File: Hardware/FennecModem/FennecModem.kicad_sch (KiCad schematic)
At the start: 8 parts, among them SW101 RESET

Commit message: Bump fennec pcb
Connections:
- net TONE_OUT: now reaches A1.4 (GPIO2)
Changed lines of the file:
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@@
+		)
+	)
+	(wire
+		(pts
+			(xy 17.78 118.11) (xy 30.48 118.11)
+		)
+		(stroke
+			(width 0)
+			(type default)
 		)
 	)
@@
 		(pts
 			(xy 262.89 135.89) (xy 262.89 139.7)
+		)
+		(stroke
+			(width 0)
+			(type default)
+		)
+	)
+	(wire
+		(pts
+			(xy 185.42 21.59) (xy 201.93 21.59)
 		)
 		(stroke
@@
 		)
 	)
+	(label "TONE_OUT"
+		(at 185.42 21.59 0)
+		(effects
+			(font
+				(size 1.27 1.27)
+			)
+			(justify left bottom)
+		)
+	)
+	(label "TONE_OUT"
+		(at 17.78 118.11 0)
+		(effects
+			(font
+				(size 1.27 1.27)
+			)
+			(justify left bottom)
+		)
+	)

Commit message: Route!
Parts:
- removed D102: SCK, LED_SMD:LED_0805_2012Metric, symbol Device:LED
- removed R107: 330, Resistor_SMD:R_0805_2012Metric, symbol Device:R
- removed SW101: RESET, Button_Switch_THT:SW_PUSH_6mm_H5mm, symbol Switch:SW_Push
- added JP2, JP3, JP4, JP5, JP6: SolderJumper_2_Open, Jumper:SolderJumper-2_P1.3mm_Open_TrianglePad1.0x1.5mm, symbol Jumper:SolderJumper_2_Open
- A1: footprint Module:RaspberryPi_Pico_Common_Unspecified -> Module:RaspberryPi_Pico_Common_THT
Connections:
- net +5V: now also A1.39 (VSYS); no longer R103.2, R108.2
- net GND: now also A1.13 (GND), A1.18 (GND), A1.23 (GND), A1.28 (GND), A1.3 (GND), A1.38 (GND), A1.8 (GND), D101.1 (K)
- net RXD: now also A1.11 (GPIO8)
- net STAT: now also A1.9 (GPIO6), R103.2; no longer D101.1 (K)
- net TXD: now also A1.12 (GPIO9)
- net PTT: now reaches A1.14 (GPIO10)
- net Sleep: now reaches A1.15 (GPIO11)
- net H/L: now reaches A1.16 (GPIO12)
- net SQL: now reaches A1.17 (GPIO13)
- net SDO: now reaches A1.21 (GPIO16)
- net CARD_SEL: now reaches A1.22 (GPIO17)
- net SPI_CLK: now reaches A1.24 (GPIO18)
- net SDI: now reaches A1.25 (GPIO19)
- net at A1.26 (GPIO20): now also JP4.2 (B)
- net at A1.27 (GPIO21): now also JP5.2 (B)
- net at A1.29 (GPIO22): now also JP6.2 (B)
- net TONE_IN: now reaches A1.31 (GPIO26_ADC0)
- net GNDA: now reaches A1.33 (AGND)
- net +3.3V: now reaches A1.36 (3V3)
- net +3.3V: now also R108.2
- net at A1.6 (GPIO4): now also JP3.2 (B)
- net at A1.7 (GPIO5): now also JP2.2 (B)
- new net SCL: JP2.1 (A)
- new net SDA: JP3.1 (A)
- new net SPI2: JP4.1 (A)
- new net SPI3: JP5.1 (A)
- new net SPI4: JP6.1 (A)
- no-connect marks 0 -> 12
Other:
- sheet Backplane ports: added CARD_SEL, SPI_SDO; removed none
- moved on the sheet: A1, D101, R103

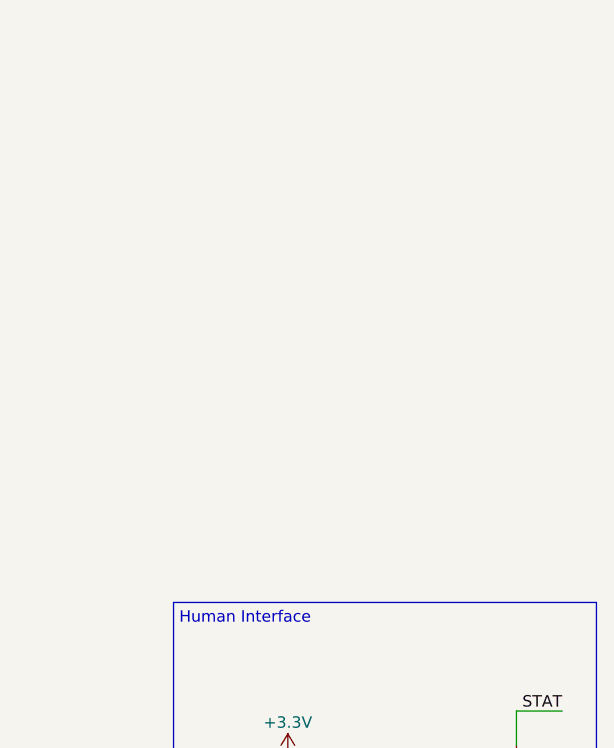
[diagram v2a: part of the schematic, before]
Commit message: Add stackup and fan
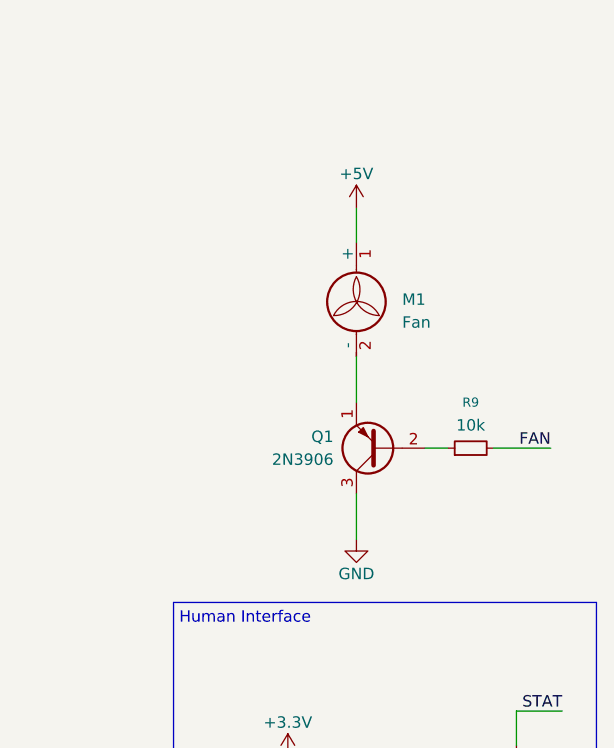
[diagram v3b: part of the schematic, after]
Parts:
- added M1: Fan, Connector_PinHeader_2.54mm:PinHeader_1x02_P2.54mm_Vertical, symbol Motor:Fan
- added Q1: 2N3906, Package_TO_SOT_THT:TO-92_Inline, symbol Transistor_BJT:2N3906
- added R9: 10k, Resistor_SMD:R_0805_2012Metric, symbol Device:R_Small
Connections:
- net +5V: now also M1.1 (+)
- net GND: now also Q1.3 (C)
- new net: M1.2 (-), Q1.1 (E)
- new net: Q1.2 (B), R9.1
- new net FAN: R9.2

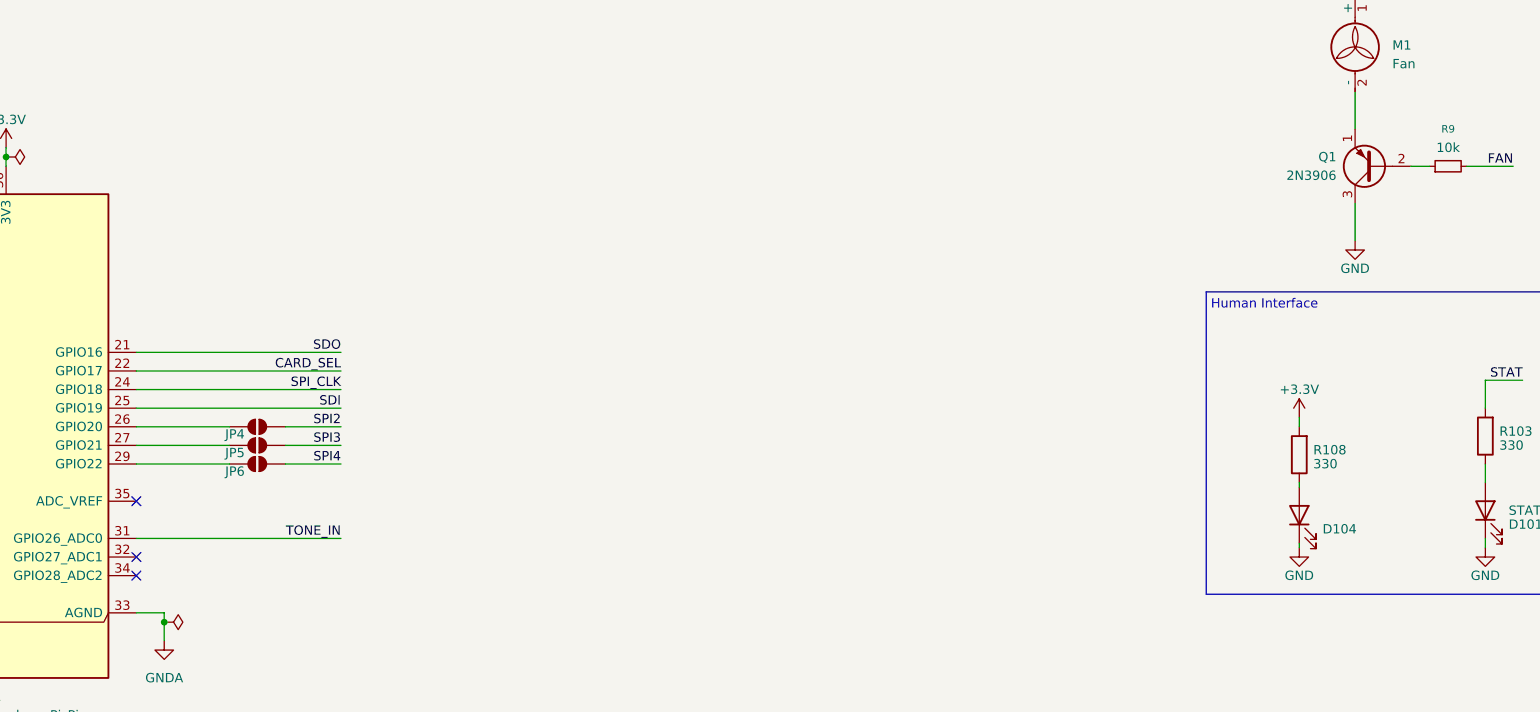
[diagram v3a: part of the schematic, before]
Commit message: Change all power switching
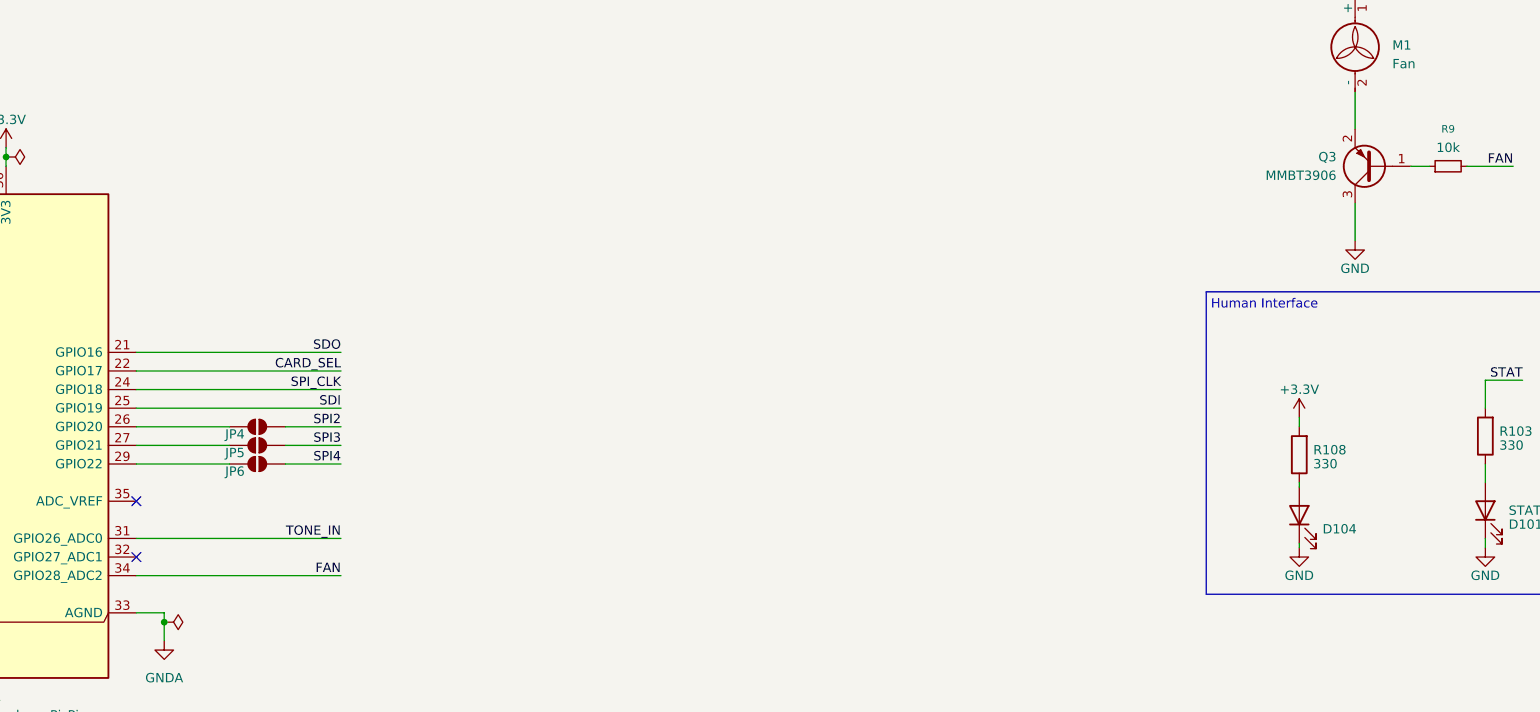
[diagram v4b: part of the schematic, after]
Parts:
- removed Q1: 2N3906, Package_TO_SOT_THT:TO-92_Inline, symbol Transistor_BJT:2N3906
- added Q3: MMBT3906, Package_TO_SOT_SMD:SOT-23, symbol Transistor_BJT:MMBT3906
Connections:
- net FAN: now also A1.34 (GPIO28_ADC2)
- net GND: now also Q3.3 (C)
- net at M1.2 (-): now also Q3.2 (E)
- net at R9.1: now also Q3.1 (B)
- no-connect marks 12 -> 11
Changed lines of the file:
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@@
-	)
-	(no_connect
-		(at 91.44 162.56)
 	)
 	(no_connect
@@
 	(wire
 		(pts
+			(xy 91.44 162.56) (xy 119.38 162.56)
+		)
+		(stroke
+			(width 0)
+			(type default)
+		)
+	)
+	(wire
+		(pts
 			(xy 185.42 21.59) (xy 201.93 21.59)
 		)
@@
 	(label "SPI_CLK"
 		(at 119.38 137.16 180)
+		(effects
+			(font
+				(size 1.27 1.27)
+			)
+			(justify right bottom)
+		)
+	)
+	(label "FAN"
+		(at 119.38 162.56 180)
 		(effects
 			(font
@@
 	)
 	(symbol
-		(lib_id "Transistor_BJT:2N3906")
-		(at 260.35 106.68 180)
-		(unit 1)
-		(exclude_from_sim no)
-		(in_bom yes)
-		(on_board yes)
-		(dnp no)
-		(fields_autoplaced yes)
-		(property "Reference" "Q1"
-			(at 255.27 105.4099 0)
-			(effects
-				(font
-					(size 1.27 1.27)
-				)
-				(justify left)
-			)
-		)
-		(property "Value" "2N3906"
-			(at 255.27 107.9499 0)
-			(effects
-				(font
-					(size 1.27 1.27)
-				)
-				(justify left)
-			)
-		)
-		(property "Footprint" "Package_TO_SOT_THT:TO-92_Inline"
-			(at 255.27 104.775 0)
-			(effects
-				(font
-					(size 1.27 1.27)
-					(italic yes)
-				)
-				(justify left)
-				(hide yes)
-			)
-		)
-		(property "Datasheet" "https://www.onsemi.com/pub/Collateral/2N3906-D.PDF"
-			(at 260.35 106.68 0)
-			(effects
-				(font
-					(size 1.27 1.27)
-				)
-				(justify left)
-				(hide yes)
-			)
-		)
-		(property "Description" "-0.2A Ic, -40V Vce, Small Signal PNP Transistor, TO-92"
-			(at 260.35 106.68 0)
-			(effects
-				(font
-					(size 1.27 1.27)
-				)
-				(hide yes)
-			)
-		)
-		(pin "2"
-		)
-		(pin "3"
-		)
-		(pin "1"
-		)
-		(instances
-			(project ""
-				(path "/8cb1f8f8-0f28-4c6f-8a0b-e6b064917aa9"
-					(reference "Q1")
-					(unit 1)
-				)
-			)
-		)
-	)
-	(symbol
 		(lib_id "Jumper:SolderJumper_2_Open")
 		(at 107.95 147.32 180)
@@
 					(unit 1)
 				)
+			)
+		)
+	)
+	(symbol
+		(lib_id "Transistor_BJT:MMBT3906")
+		(at 260.35 106.68 180)
+		(unit 1)
+		(exclude_from_sim no)
+		(in_bom yes)
+		(on_board yes)
+		(dnp no)
+		(fields_autoplaced yes)
+		(property "Reference" "Q3"
+			(at 255.27 105.4099 0)
+			(effects
+				(font
+					(size 1.27 1.27)
+				)
+				(justify left)
+			)
+		)
+		(property "Value" "MMBT3906"
+			(at 255.27 107.9499 0)
+			(effects
+				(font
+					(size 1.27 1.27)
+				)
+				(justify left)
+			)
+		)
+		(property "Footprint" "Package_TO_SOT_SMD:SOT-23"
+			(at 255.27 104.775 0)
+			(effects
+				(font
+					(size 1.27 1.27)
+					(italic yes)
+				)
+				(justify left)
+				(hide yes)
+			)
+		)
+		(property "Datasheet" "https://www.onsemi.com/pdf/datasheet/pzt3906-d.pdf"
+			(at 260.35 106.68 0)
+			(effects
+				(font
+					(size 1.27 1.27)
+				)
+				(justify left)
+				(hide yes)
+			)
+		)
+		(property "Description" "-0.2A Ic, -40V Vce, Small Signal PNP Transistor, SOT-23"
+			(at 260.35 106.68 0)
+			(effects
+				(font
+					(size 1.27 1.27)
+				)
+				(hide yes)
+			)
+		)
+		(pin "2"
+		)
+		(pin "3"
+		)
+		(pin "1"
+		)
+		(instances
+			(project ""
+				(path "/8cb1f8f8-0f28-4c6f-8a0b-e6b064917aa9"
+					(reference "Q3")
+					(unit 1)
+				)

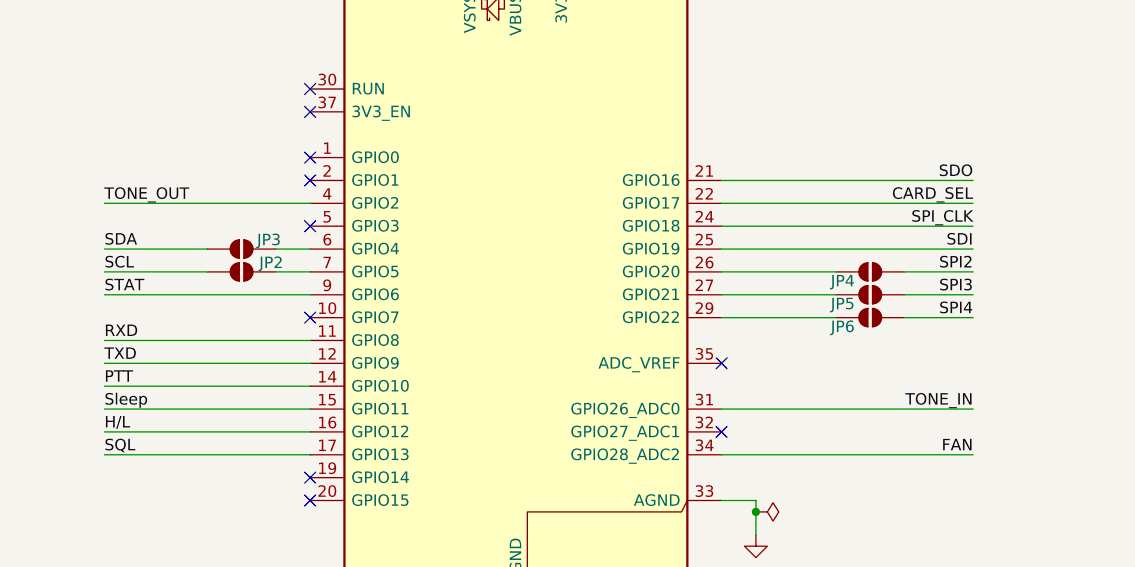
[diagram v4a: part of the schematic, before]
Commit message: Add all nets
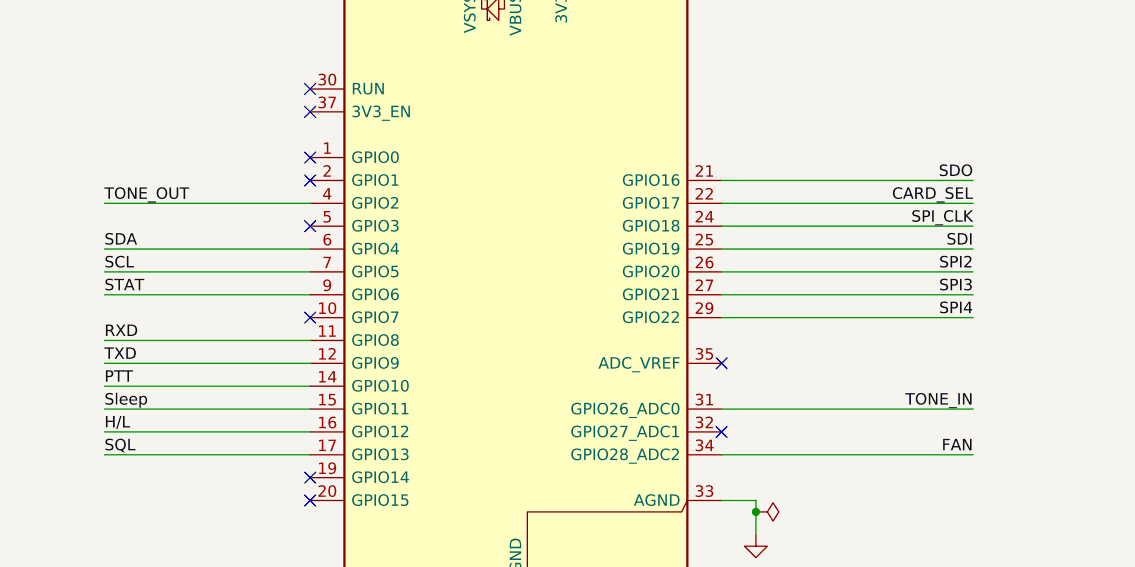
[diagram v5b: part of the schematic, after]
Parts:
- removed JP2, JP3, JP4, JP5, JP6: SolderJumper_2_Open, Jumper:SolderJumper-2_P1.3mm_Open_TrianglePad1.0x1.5mm, symbol Jumper:SolderJumper_2_Open
- M1: footprint Connector_PinHeader_2.54mm:PinHeader_1x02_P2.54mm_Vertical -> Connector_JST:JST_EH_B2B-EH-A_1x02_P2.50mm_Vertical
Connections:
- net SCL: now also A1.7 (GPIO5)
- net SDA: now also A1.6 (GPIO4)
- net SPI2: now also A1.26 (GPIO20)
- net SPI3: now also A1.27 (GPIO21)
- net SPI4: now also A1.29 (GPIO22)

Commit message: Implement suggestions from KA2
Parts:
- added C1: 1μf, Capacitor_SMD:C_0805_2012Metric, symbol Device:C_Small
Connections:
- net +5V: now also C1.1
- net at M1.2 (-), Q3.2 (E): now also C1.2
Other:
- note added: "Reccomended to prevent noise on RX"
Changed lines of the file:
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@@
 		(comment 4 "${FULL_REVISION}")
+	)
+	(text "Reccomended\nto prevent\nnoise on RX"
+		(exclude_from_sim no)
+		(at 270.256 93.218 0)
+		(effects
+			(font
+				(size 1.27 1.27)
+			)
+			(justify left top)
+		)
 	)
 	(text "Human Interface"
@@
 			(justify left bottom)
 		)
+	)
+	(junction
+		(at 257.81 82.55)
+		(diameter 0)
+		(color 0 0 0 0)
 	)
 	(junction
@@
 	)
 	(junction
+		(at 257.81 97.79)
+		(diameter 0)
+		(color 0 0 0 0)
+	)
+	(junction
 		(at 95.25 168.91)
 		(diameter 0)
@@
 	(wire
 		(pts
-			(xy 257.81 96.52) (xy 257.81 101.6)
+			(xy 257.81 96.52) (xy 257.81 97.79)
 		)
 		(stroke
@@
 	(wire
 		(pts
-			(xy 257.81 80.01) (xy 257.81 83.82)
+			(xy 257.81 80.01) (xy 257.81 82.55)
 		)
 		(stroke
@@
 	(wire
 		(pts
+			(xy 257.81 97.79) (xy 269.24 97.79)
+		)
+		(stroke
+			(width 0)
+			(type default)
+		)
+	)
+	(wire
+		(pts
 			(xy 275.59 157.48) (xy 275.59 158.75)
 		)
@@
 	(wire
 		(pts
+			(xy 269.24 97.79) (xy 269.24 92.71)
+		)
+		(stroke
+			(width 0)
+			(type default)
+		)
+	)
+	(wire
+		(pts
 			(xy 245.11 27.94) (xy 255.27 27.94)
 		)
@@
 	(wire
 		(pts
+			(xy 257.81 97.79) (xy 257.81 101.6)
+		)
+		(stroke
+			(width 0)
+			(type default)
+		)
+	)
+	(wire
+		(pts
+			(xy 269.24 87.63) (xy 269.24 82.55)
+		)
+		(stroke
+			(width 0)
+			(type default)
+		)
+	)
+	(wire
+		(pts
+			(xy 269.24 82.55) (xy 257.81 82.55)
+		)
+		(stroke
+			(width 0)
+			(type default)
+		)
+	)
+	(wire
+		(pts
 			(xy 91.44 162.56) (xy 119.38 162.56)
 		)
@@
 		(pts
 			(xy 250.19 41.91) (xy 252.095 43.815)
+		)
+		(stroke
+			(width 0)
+			(type default)
+		)
+	)
+	(wire
+		(pts
+			(xy 257.81 82.55) (xy 257.81 83.82)
 		)
 		(stroke
@@
 					(unit 1)
 				)
+			)
+		)
+	)
+	(symbol
+		(lib_id "Device:C_Small")
+		(at 269.24 90.17 0)
+		(unit 1)
+		(exclude_from_sim no)
+		(in_bom yes)
+		(on_board yes)
+		(dnp no)
+		(fields_autoplaced yes)
+		(property "Reference" "C1"
+			(at 271.78 88.9062 0)
+			(effects
+				(font
+					(size 1.27 1.27)
+				)
+				(justify left)
+			)
+		)
+		(property "Value" "1μf"
+			(at 271.78 91.4462 0)
+			(effects
+				(font
+					(size 1.27 1.27)
+				)
+				(justify left)
+			)
+		)
+		(property "Footprint" "Capacitor_SMD:C_0805_2012Metric"
+			(at 269.24 90.17 0)
+			(effects
+				(font
+					(size 1.27 1.27)
+				)
+				(hide yes)
+			)
+		)
+		(property "Datasheet" "~"
+			(at 269.24 90.17 0)
+			(effects
+				(font
+					(size 1.27 1.27)
+				)
+				(hide yes)
+			)
+		)
+		(property "Description" ""
+			(at 269.24 90.17 0)
+			(effects
+				(font
+					(size 1.27 1.27)
+				)
+			)
+		)
+		(pin "1"
+		)
+		(pin "2"
+		)
+		(instances
+			(project "FennecModem"
+				(path "/8cb1f8f8-0f28-4c6f-8a0b-e6b064917aa9"
+					(reference "C1")
+					(unit 1)
+				)
